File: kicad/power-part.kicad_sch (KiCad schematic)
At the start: 52 parts, among them Q10 BSS84, Q11 BSS123N, Q12 ZXMP10A17GTA, Q2 IPT015N10N5, Q3 IPT015N10N5, Q4 IPT015N10N5, Q5 IPT015N10N5, Q6 IPT015N10N5, Q7 IPT015N10N5, Q8 IPT015N10N5, Q9 IPT015N10N5

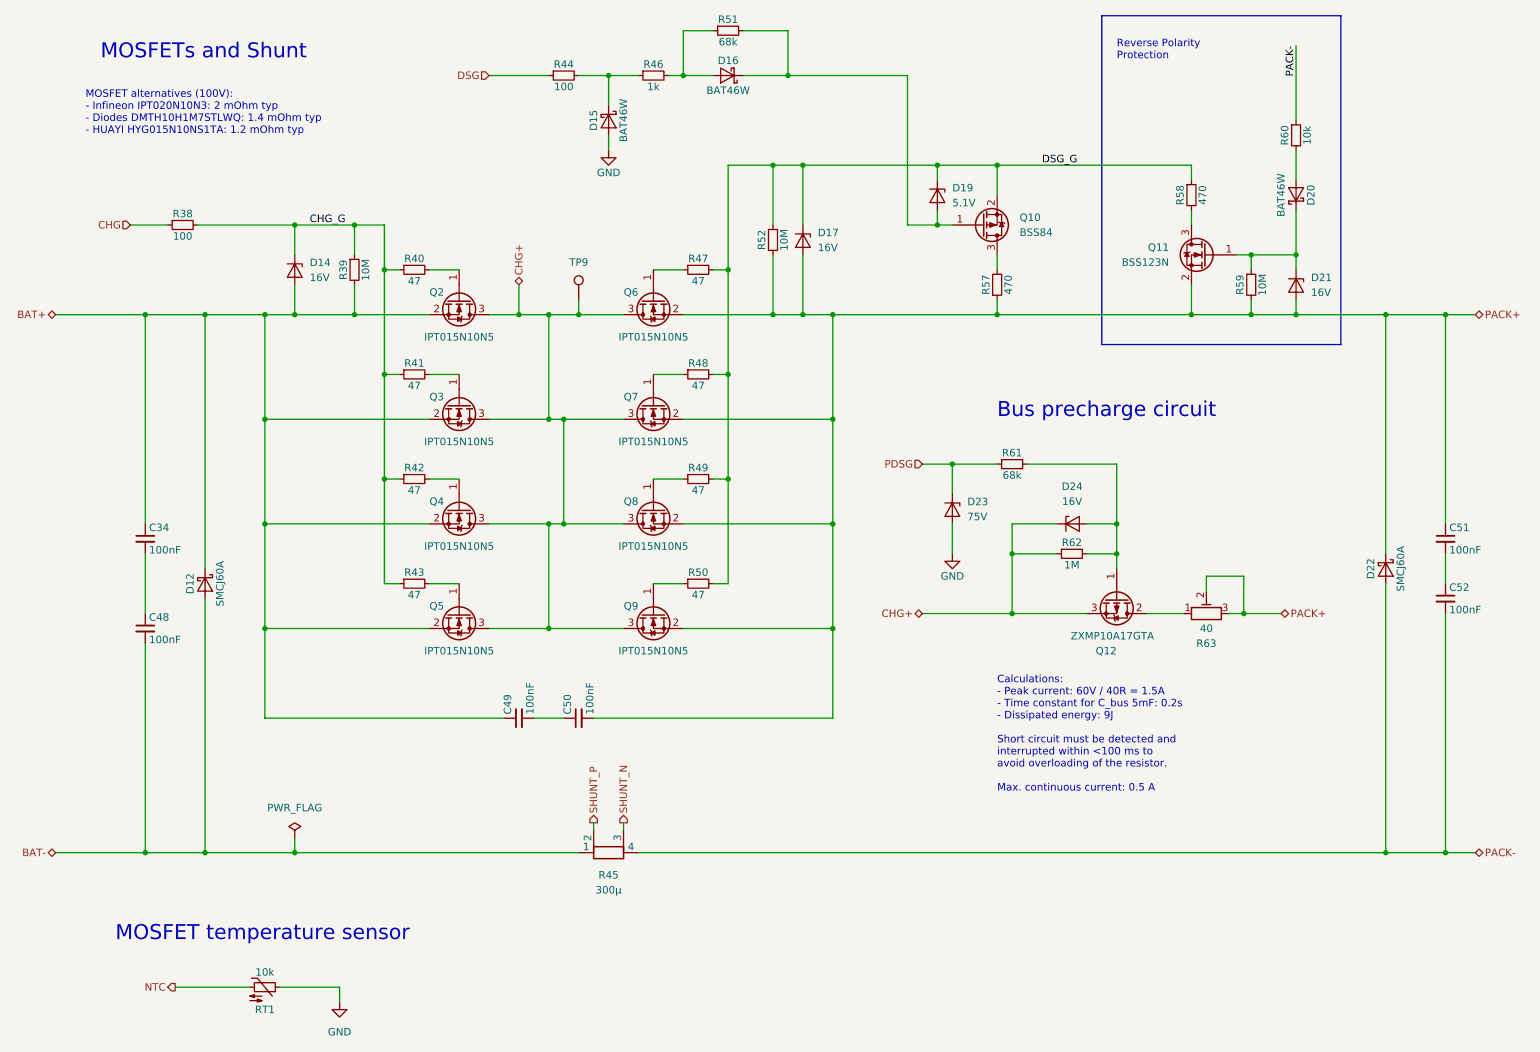
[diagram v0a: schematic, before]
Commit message: v0.4.0: Multiple improvements for new board revision
- Use LMR38010 for internal power supply (max. 80V instead of 60V)
- Change USB connector from Micro-A to C and remove 5V power supply
  which was not working anyway. The board cannot be powered by USB
  only.
- Add TS2 (connected to DFETOFF) to measure shunt temperature
- Add RS-485 transceiver (sharing the connector with CAN)
- Switch I2C pins of ESP32-C3 to GPIO8/9. This allows to re-use the
  I2C pull-ups for strapping configuration and frees two pins for the
  RS-485 transceiver RE and DE pins. Also we may get rid of the I2C
  glitches during start-up.
- Reduce DSG gate resistor R57 to 47R to increase switch-off speed.
- Use more easily available and cheaper Würth 7466005R terminals with
  countersunk hole/thread.
- Adjust some resistors to reduce number of different parts
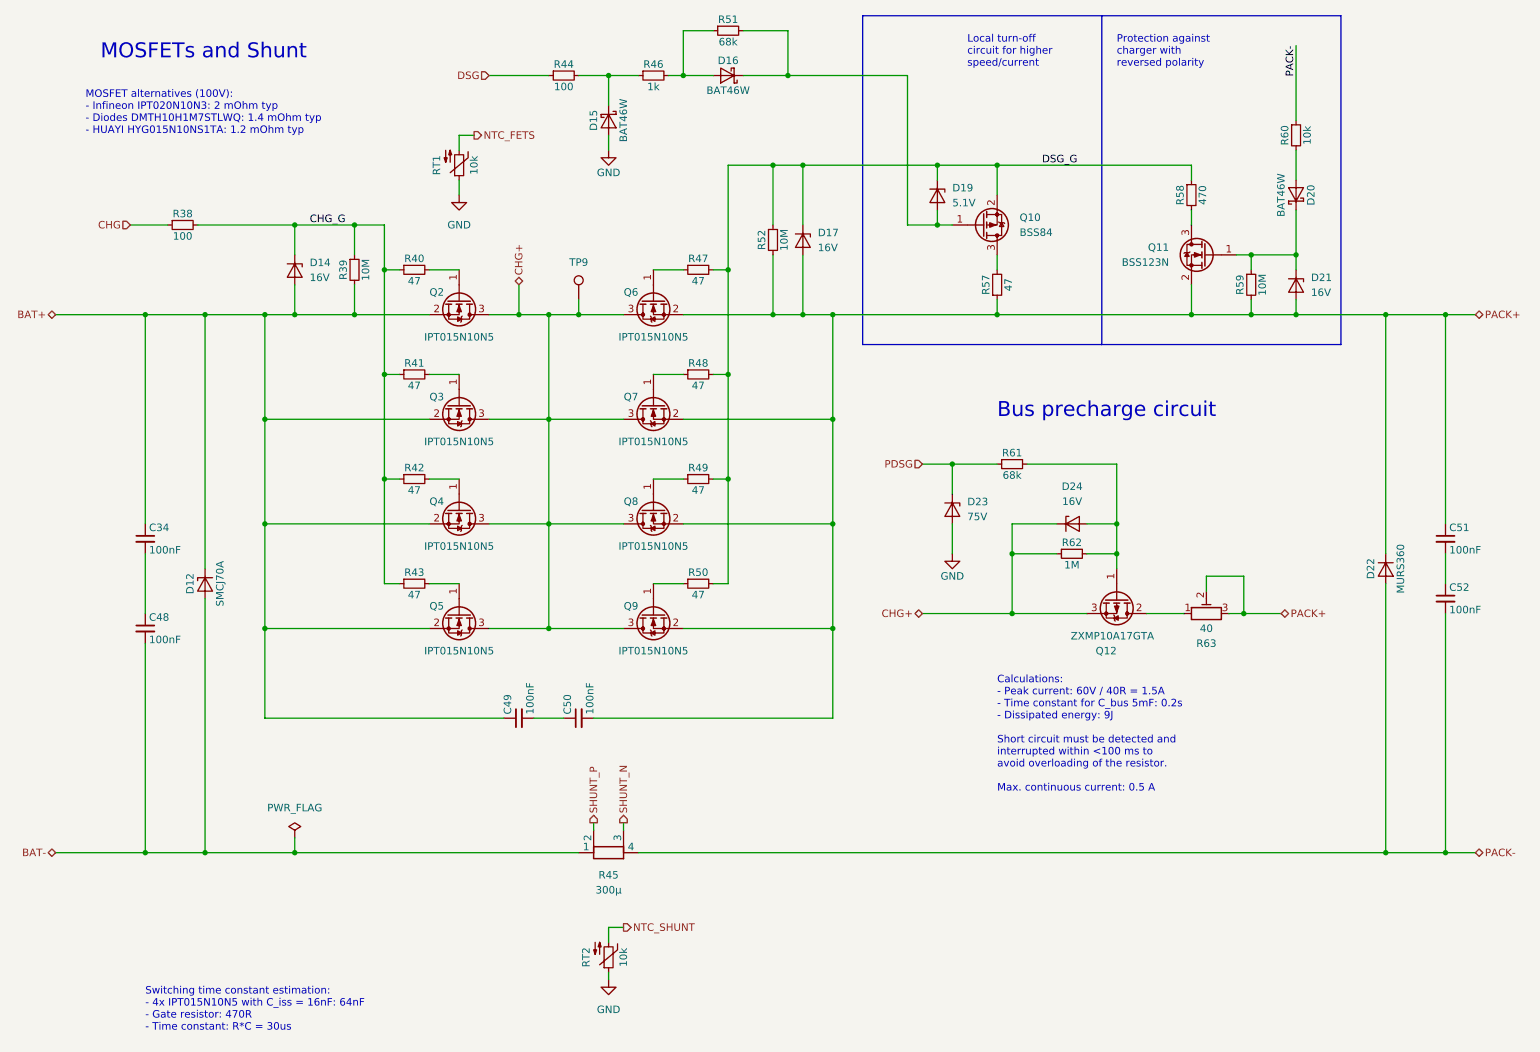
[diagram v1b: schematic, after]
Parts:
- added RT2: 10k, LibreSolar:R_0603_1608, symbol LibreSolar:R_NTC
- D12: value SMCJ60A -> SMCJ70A; symbol LibreSolar:D_Schottky -> LibreSolar:D_Zener; PartNumber SMCJ60A -> SMCJ70A; Remarks Alternative: Diodes Inc. SMCJ60A-13-F -> Alternative: Diodes Inc. SMCJ70A-13-F
- D22: value SMCJ60A -> MURS360; symbol LibreSolar:D_Schottky -> LibreSolar:D; Manufacturer Bourns -> Diodes Incorporated; PartNumber SMCJ60A -> MURS360; Remarks Alternative: Diodes Inc. SMCJ60A-13-F -> Alternative: Other MURS360
- R57: value 470 -> 47
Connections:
- net GND: now also RT2.1
- net NTC renamed NTC_FETS
- new net NTC_SHUNT: RT2.2
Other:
- note added: "Local turn-off circuit for higher speed/current"
- note added: "Protection against charger with reversed polarity"
- note added: "Switching time constant estimation: - 4x IPT015N10N5 with C_iss = 16nF: 64nF - Gate resistor: 470R - Time constant: R*C = 30us"
- note removed: "MOSFET temperature sensor"
- note removed: "Reverse Polarity Protection"
- moved on the sheet: RT1
